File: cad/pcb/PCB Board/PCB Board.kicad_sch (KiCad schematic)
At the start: 14 parts, among them J1 Conn_01x02_Pin, J2 Conn_01x03_Pin, J3 Conn_01x04_Pin, J4 Conn_01x03_Pin, Q1 BC547, Q2 BC547, Q3 BC547, SW1 SW_Push, SW2 SW_Push, SW3 SW_Push, SW4 SW_Push

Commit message: started work on the pcb and cad data
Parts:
- removed J3: Conn_01x04_Pin, Connector_JST:JST_XH_B4B-XH-A_1x04_P2.50mm_Vertical, symbol Connector:Conn_01x04_Pin
- removed J4: Conn_01x03_Pin, Connector_JST:JST_XH_B3B-XH-A_1x03_P2.50mm_Vertical, symbol Connector:Conn_01x03_Pin
- removed Q1, Q2, Q3: BC547, Package_TO_SOT_THT:TO-92_Inline, symbol Transistor_BJT:BC547
- removed R1, R2, R3: R33K, Resistor_THT:R_Axial_DIN0204_L3.6mm_D1.6mm_P7.62mm_Horizontal, symbol Device:R
- added J3: Conn_01x02_Pin, Connector_Wire:SolderWire-0.1sqmm_1x02_P3.6mm_D0.4mm_OD1mm, symbol Connector:Conn_01x02_Pin
- added StepUp1: ~, Library:StepUp, symbol ReactPod:StepUp
- added U1: BOB-12009, BOB-12009:CONV_BOB-12009, symbol BOB-12009:BOB-12009
- added U2: ~, Library:Lolin32 Lite, symbol ReactPod:Lolin32
- J1: value Conn_01x02_Pin -> POWER
- J2: value Conn_01x03_Pin -> LED+
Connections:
- net at SW1.1, SW2.1, SW3.1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: now also J1.2 (Pin_2), J3.2 (Pin_2), StepUp1.1 (IN-), U1.GND_1 (GND), U1.GND_2 (GND), U2.GND
- net at SW1.2, SW2.2, SW3.2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: now also U2.18; no longer J1.2 (Pin_2)
- new net: J1.1 (Pin_1), J3.1 (Pin_1), StepUp1.2 (IN+)
- new net: J2.1 (Pin_1), U1.HV1
- new net: J2.2 (Pin_2), StepUp1.4 (OUT-)
- new net: J2.3 (Pin_3), StepUp1.3 (OUT+), U1.HV
- new net: U1.LV1, U2.19
- new net: U1.LV, U2.3V
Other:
- moved on the sheet: J2, SW1, SW2, SW3, SW4

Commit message: updated pcbs
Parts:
- added J4: ON_OFF_SWITCH, Connector_Wire:SolderWire-0.1sqmm_1x02_P3.6mm_D0.4mm_OD1mm_Relief, symbol Connector:Conn_01x02_Pin
- J3: value Conn_01x02_Pin -> BATTERY_CONNECTOR
- U1: value BOB-12009 -> Lvl-Shifter
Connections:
- net at J3.1 (Pin_1), StepUp1.2 (IN+): now also J4.1 (Pin_1); no longer J1.1 (Pin_1)
- new net: J1.1 (Pin_1), J4.2 (Pin_2)
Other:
- moved on the sheet: J1
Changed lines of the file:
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@@
 	(wire
 		(pts
-			(xy 12.7 33.02) (xy 12.7 157.48)
+			(xy 12.7 31.75) (xy 12.7 157.48)
 		)
 		(stroke
@@
 	(wire
 		(pts
-			(xy 46.99 30.48) (xy 48.26 30.48)
-		)
-		(stroke
-			(width 0)
-			(type default)
-		)
-	)
-	(wire
-		(pts
-			(xy 12.7 33.02) (xy 48.26 33.02)
+			(xy 19.05 24.13) (xy 48.26 24.13)
+		)
+		(stroke
+			(width 0)
+			(type default)
+		)
+	)
+	(wire
+		(pts
+			(xy 12.7 31.75) (xy 48.26 31.75)
 		)
 		(stroke
@@
 	(wire
 		(pts
-			(xy 48.26 26.67) (xy 57.15 26.67)
-		)
-		(stroke
-			(width 0)
-			(type default)
-		)
-	)
-	(wire
-		(pts
 			(xy 40.64 78.74) (xy 62.23 78.74)
 		)
@@
 	(wire
 		(pts
+			(xy 29.21 21.59) (xy 19.05 21.59)
+		)
+		(stroke
+			(width 0)
+			(type default)
+		)
+	)
+	(wire
+		(pts
 			(xy 69.85 173.99) (xy 62.23 173.99)
 		)
@@
 	(wire
 		(pts
-			(xy 48.26 27.94) (xy 48.26 26.67)
+			(xy 57.15 21.59) (xy 57.15 26.67)
 		)
 		(stroke
@@
 	(wire
 		(pts
-			(xy 46.99 27.94) (xy 48.26 27.94)
-		)
-		(stroke
-			(width 0)
-			(type default)
-		)
-	)
-	(wire
-		(pts
 			(xy 62.23 31.75) (xy 125.73 31.75)
 		)
@@
 	(wire
 		(pts
+			(xy 31.75 21.59) (xy 57.15 21.59)
+		)
+		(stroke
+			(width 0)
+			(type default)
+		)
+	)
+	(wire
+		(pts
 			(xy 157.48 26.67) (xy 189.23 26.67)
 		)
@@
 	(wire
 		(pts
-			(xy 48.26 33.02) (xy 48.26 31.75)
-		)
-		(stroke
-			(width 0)
-			(type default)
-		)
-	)
-	(wire
-		(pts
 			(xy 57.15 76.2) (xy 57.15 26.67)
 		)
@@
 	(wire
 		(pts
-			(xy 48.26 30.48) (xy 48.26 31.75)
+			(xy 48.26 24.13) (xy 48.26 31.75)
 		)
 		(stroke
@@
 		(length 2.54)
 		(shape round)
-		(at 29.21 33.02 0)
+		(at 29.21 31.75 0)
 		(fields_autoplaced yes)
 		(effects
@@
 		)
 		(property "Netclass" "GND"
-			(at 29.9085 30.48 0)
+			(at 29.9085 29.21 0)
 			(effects
 				(font
@@
 			)
 		)
-		(property "Value" "Conn_01x02_Pin"
+		(property "Value" "BATTERY_CONNECTOR"
 			(at 36.195 73.66 0)
 			(effects
@@
 	(symbol
 		(lib_id "Connector:Conn_01x02_Pin")
-		(at 41.91 27.94 0)
+		(at 31.75 16.51 270)
+		(unit 1)
+		(exclude_from_sim no)
+		(in_bom yes)
+		(on_board yes)
+		(dnp no)
+		(fields_autoplaced yes)
+		(property "Reference" "J4"
+			(at 33.02 15.8749 90)
+			(effects
+				(font
+					(size 1.27 1.27)
+				)
+				(justify left)
+			)
+		)
+		(property "Value" "ON_OFF_SWITCH"
+			(at 33.02 18.4149 90)
+			(effects
+				(font
+					(size 1.27 1.27)
+				)
+				(justify left)
+			)
+		)
+		(property "Footprint" "Connector_Wire:SolderWire-0.1sqmm_1x02_P3.6mm_D0.4mm_OD1mm_Relief"
+			(at 31.75 16.51 0)
+			(effects
+				(font
+					(size 1.27 1.27)
+				)
+				(hide yes)
+			)
+		)
+		(property "Datasheet" "~"
+			(at 31.75 16.51 0)
+			(effects
+				(font
+					(size 1.27 1.27)
+				)
+				(hide yes)
+			)
+		)
+		(property "Description" "Generic connector, single row, 01x02, script generated"
+			(at 31.75 16.51 0)
+			(effects
+				(font
+					(size 1.27 1.27)
+				)
+				(hide yes)
+			)
+		)
+		(pin "1"
+		)
+		(pin "2"
+		)
+		(instances
+			(project "PCB Board"
+				(path "/fdfca3f3-2f26-422d-bb5a-3dc9ec4c075c"
+					(reference "J4")
+					(unit 1)
+				)
+			)
+		)
+	)
+	(symbol
+		(lib_id "Connector:Conn_01x02_Pin")
+		(at 13.97 21.59 0)
 		(unit 1)
 		(exclude_from_sim no)
@@
 		(fields_autoplaced yes)
 		(property "Reference" "J1"
-			(at 42.545 22.86 0)
+			(at 14.605 16.51 0)
 			(effects
 				(font
@@
 		)
 		(property "Value" "POWER"
-			(at 42.545 25.4 0)
+			(at 14.605 19.05 0)
 			(effects
 				(font
@@
 		)
 		(property "Footprint" "Connector_JST:JST_XH_B2B-XH-A_1x02_P2.50mm_Vertical"
-			(at 41.91 27.94 0)
+			(at 13.97 21.59 0)
 			(effects
 				(font
@@
 		)
 		(property "Datasheet" "~"
-			(at 41.91 27.94 0)
+			(at 13.97 21.59 0)
 			(effects
 				(font
@@
 		)
 		(property "Description" "Generic connector, single row, 01x02, script generated"
-			(at 41.91 27.94 0)
+			(at 13.97 21.59 0)
 			(effects
 				(font
@@
 			)
 		)
-		(property "Value" "BOB-12009"
+		(property "Value" "Lvl-Shifter"
 			(at 166.37 76.2 0)
 			(effects

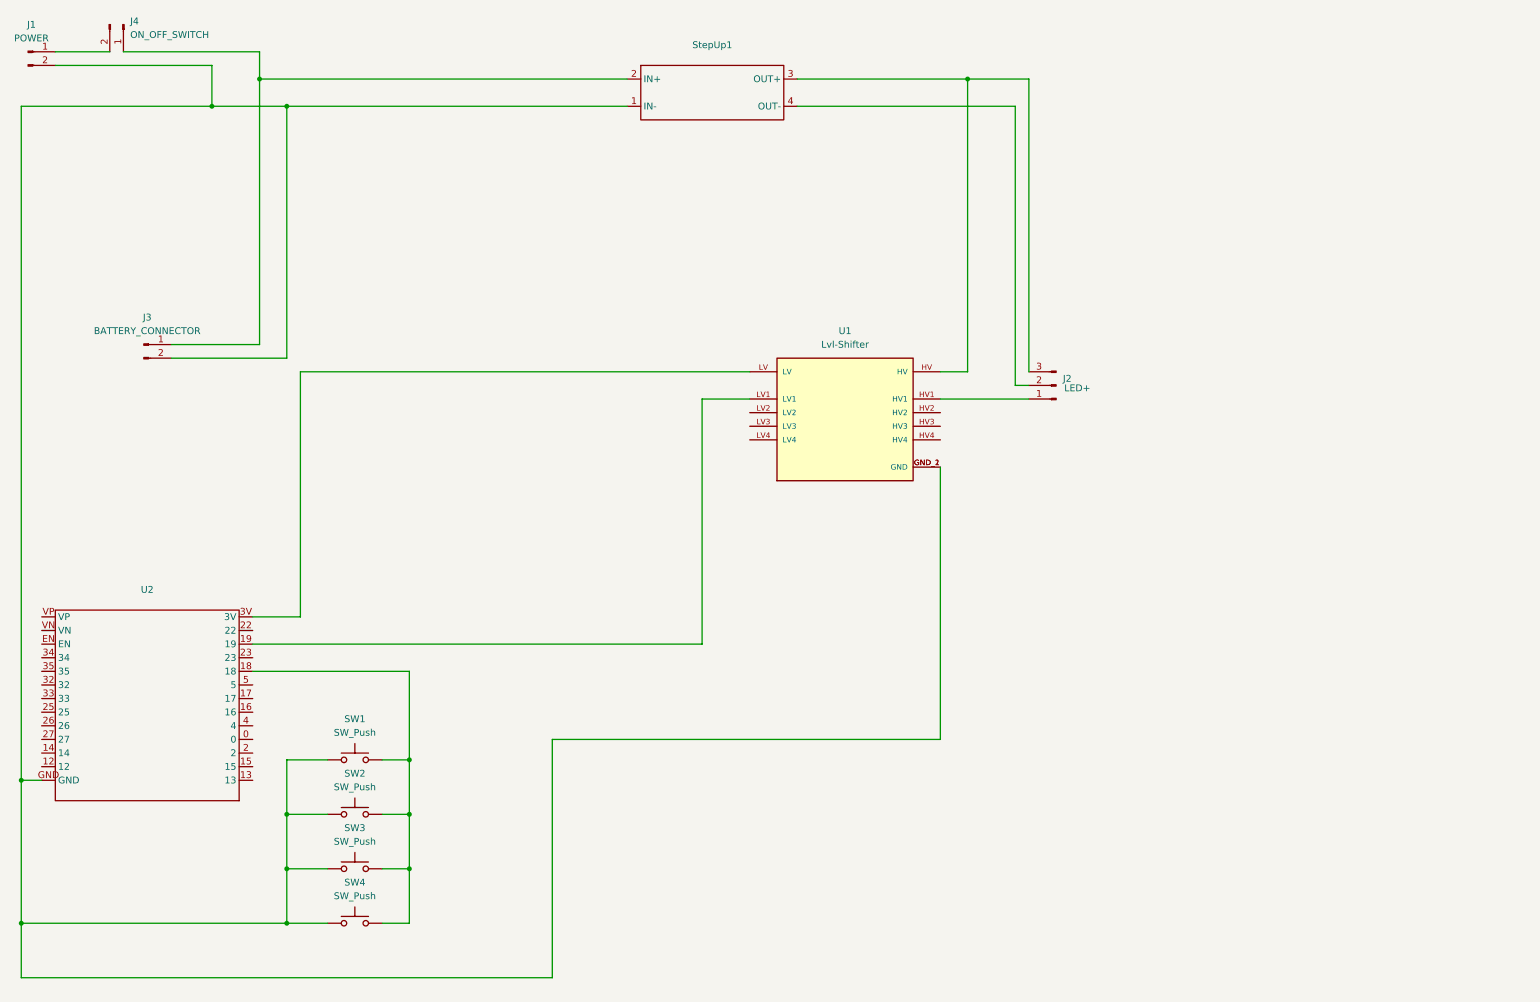
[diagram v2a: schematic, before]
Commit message: updated pcb design schematic
layouting missing. Also add on/off switch for battery (best solution with circumventing switch on charge
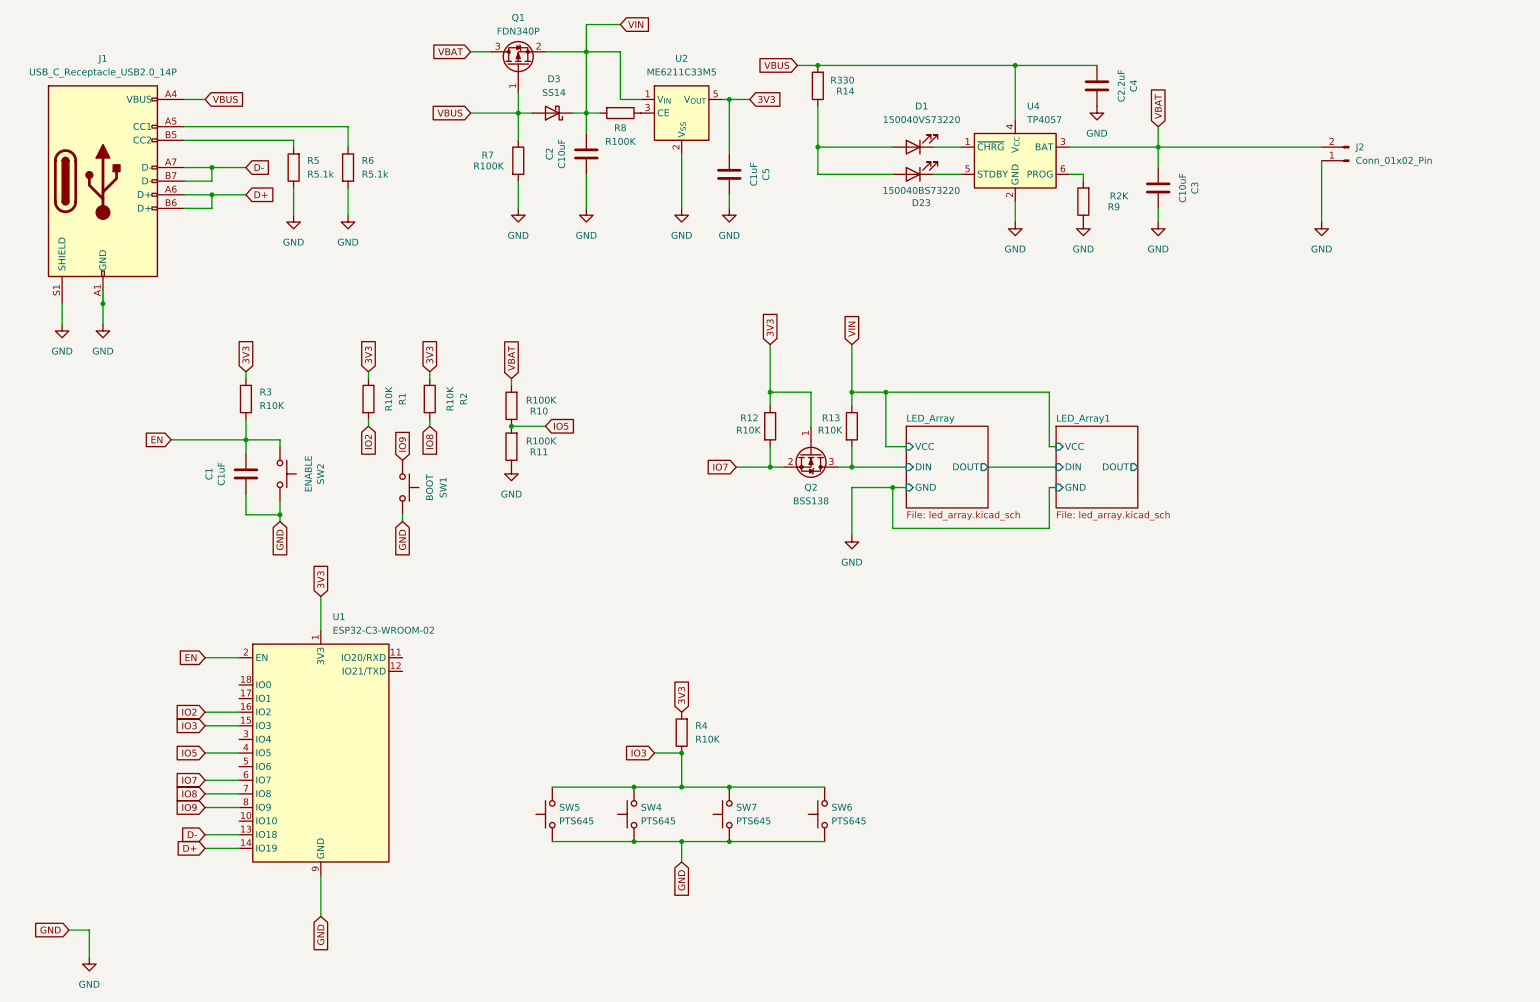
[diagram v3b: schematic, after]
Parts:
- removed J1: POWER, Connector_JST:JST_XH_B2B-XH-A_1x02_P2.50mm_Vertical, symbol Connector:Conn_01x02_Pin
- removed J2: LED+, Connector_JST:JST_XH_B3B-XH-A_1x03_P2.50mm_Vertical, symbol Connector:Conn_01x03_Pin
- removed J3: BATTERY_CONNECTOR, Connector_Wire:SolderWire-0.1sqmm_1x02_P3.6mm_D0.4mm_OD1mm, symbol Connector:Conn_01x02_Pin
- removed J4: ON_OFF_SWITCH, Connector_Wire:SolderWire-0.1sqmm_1x02_P3.6mm_D0.4mm_OD1mm_Relief, symbol Connector:Conn_01x02_Pin
- removed SW3: SW_Push, Button_Switch_THT:SW_PUSH_6mm_H5mm, symbol Switch:SW_Push
- removed StepUp1: ~, Library:StepUp, symbol ReactPod:StepUp
- removed U1: Lvl-Shifter, BOB-12009:CONV_BOB-12009, symbol BOB-12009:BOB-12009
- removed U2: ~, Library:Lolin32 Lite, symbol ReactPod:Lolin32
- added C1, C5: C1uF, Capacitor_SMD:C_0402_1005Metric, symbol Device:C
- added C2, C3: C10uF, Capacitor_SMD:C_0402_1005Metric, symbol Device:C
- added C4: C2.2uF, Capacitor_SMD:C_0402_1005Metric, symbol Device:C
- added D1: 150040VS73220, LED_SMD:LED_0402_1005Metric, symbol Device:LED
- added D23: 150040BS73220, LED_SMD:LED_0402_1005Metric, symbol Device:LED
- added D3: SS14, Diode_SMD:D_SMA, symbol Diode:SS14
- added J1: USB_C_Receptacle_USB2.0_14P, Connector_USB:USB_C_Receptacle_GCT_USB4105-xx-A_16P_TopMnt_Horizontal, symbol Connector:USB_C_Receptacle_USB2.0_14P
- added J2: Conn_01x02_Pin, Connector_JST:JST_PH_S2B-PH-K_1x02_P2.00mm_Horizontal, symbol Connector:Conn_01x02_Pin
- added Q1: FDN340P, Package_TO_SOT_SMD:SOT-23, symbol Transistor_FET:FDN340P
- added Q2: BSS138, Package_TO_SOT_SMD:SOT-23, symbol Transistor_FET:BSS138
- added R1, R12, R13, R2, R3, R4: R10K, Resistor_SMD:R_0402_1005Metric, symbol Device:R
- added R10, R11, R7, R8: R100K, Resistor_SMD:R_0402_1005Metric, symbol Device:R
- added R14: R330, Resistor_SMD:R_0402_1005Metric, symbol Device:R
- added R5, R6: R5.1k, Resistor_SMD:R_0402_1005Metric, symbol Device:R
- added R9: R2K, Resistor_SMD:R_0402_1005Metric, symbol Device:R
- added SW5, SW6, SW7: PTS645, Button_Switch_SMD:SW_SPST_PTS645, symbol Switch:SW_Push
- added U1: ESP32-C3-WROOM-02, RF_Module:ESP32-C3-WROOM-02, symbol RF_Module:ESP32-C3-WROOM-02
- added U2: ME6211C33M5, Package_TO_SOT_SMD:SOT-23-5, symbol Regulator_Linear:ME6211C33M5
- added U4: TP4057, Package_TO_SOT_SMD:TSOT-23-6, symbol Battery_Management:TP4057
- SW1: value SW_Push -> BOOT; footprint Button_Switch_THT:SW_PUSH_6mm_H5mm -> (none)
- SW2: value SW_Push -> ENABLE; footprint Button_Switch_THT:SW_PUSH_6mm_H5mm -> (none)
- SW4: value SW_Push -> PTS645; footprint Button_Switch_THT:SW_PUSH_6mm_H5mm -> Button_Switch_SMD:SW_SPST_PTS645
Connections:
- net GND: now reaches SW1.1, SW4.1
- net GND: now also SW2.2, C1.1, C2.1, C3.2, C4.2, C5.2, J1.A1 (GND), J1.A12 (GND), J1.B1 (GND), J1.B12 (GND), J1.S1 (SHIELD), J2.1 (Pin_1), R11.1, R5.1, R6.2, R7.2, R9.1, SW5.1, SW6.1, SW7.1, U1.19 (GND), U1.9 (GND), U2.2 (V_{SS}), U4.2 (GND); no longer SW2.1
- new net: J1.A5 (CC1), R6.1
- new net: J1.B5 (CC2), R5.2
- new net: R8.1, U2.3 (CE)
- new net: D1.1 (K), U4.1 (~{CHRG})
- new net: D23.1 (K), U4.5 (STDBY)
- new net: R9.2, U4.6 (PROG)
- new net: D1.2 (A), D23.2 (A), R14.1
- new net 3V3: C5.1, Q2.1 (G), R1.1, R12.1, R2.1, R3.2, R4.2, U1.1 (3V3), U2.5 (V_{OUT})
- new net D+: J1.A6 (D+), J1.B6 (D+), U1.14 (IO19)
- new net D-: J1.A7 (D-), J1.B7 (D-), U1.13 (IO18)
- new net EN: C1.2, R3.1, SW2.1, U1.2 (EN)
- new net IO2: R1.2, U1.16 (IO2)
- new net IO3: R4.1, SW4.2, SW5.2, SW6.2, SW7.2, U1.15 (IO3)
- new net IO5: R10.1, R11.2, U1.4 (IO5)
- new net IO7: Q2.2 (S), R12.2, U1.6 (IO7)
- new net IO8: R2.2, U1.7 (IO8)
- new net IO9: SW1.2, U1.8 (IO9)
- new net LED_Array/DIN: Q2.3 (D), R13.2
- new net VBAT: C3.1, J2.2 (Pin_2), Q1.3 (D), R10.2, U4.3 (BAT)
- new net VBUS: C4.1, D3.2 (A), J1.A4 (VBUS), J1.A9 (VBUS), J1.B4 (VBUS), J1.B9 (VBUS), Q1.1 (G), R14.2, R7.1, U4.4 (V_{CC})
- new net VIN: C2.2, D3.1 (K), Q1.2 (S), R13.1, R8.2, U2.1 (V_{IN})
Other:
- added sheet LED_Array (led_array.kicad_sch)
- added sheet LED_Array1 (led_array.kicad_sch)

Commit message: [WIP] save changes
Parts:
- added H2, H3, H4: MountingHole_Pad, MountingHole:MountingHole_3.2mm_M3_DIN965_Pad_TopBottom, symbol Mechanical:MountingHole_Pad
- added R14: R470, Resistor_SMD:R_0402_1005Metric, symbol Device:R
- added SW7: SLW-1277545-3A-RA-N-D, Button_Switch_THT:SW_Slide_SPDT_Angled_CK_OS102011MA1Q, symbol Switch:SW_Wuerth_450301014042
- C1: LCSC (none) -> C14445
- C2: LCSC (none) -> C77000
- C3: renamed from C5; LCSC (none) -> C14445
- C4: LCSC (none) -> C60078
- C5: renamed from C3; LCSC (none) -> C77000
- D1: renamed from D3; LCSC (none) -> C168859
- D2: renamed from D1; LCSC (none) -> C965793
- D3: renamed from D23; LCSC (none) -> C130724
- J1: value USB_C_Receptacle_USB2.0_14P -> USB4105
- J2: value Conn_01x02_Pin -> S2B-PH-K-S; LCSC (none) -> C173752
- SW1: renamed from SW2; value ENABLE -> PTS645; footprint (none) -> Button_Switch_SMD:SW_SPST_PTS645
- SW2: renamed from SW1; value BOOT -> PTS645; footprint (none) -> Button_Switch_SMD:SW_SPST_PTS645
- U2: value ME6211C33M5 -> TLV75533PDYDR; AltMPN (none) -> ME6211C33M5
- renumbered R3 to R1, R4 to R10, R14 to R11, R9 to R15, R5 to R2, R6 to R3, R1 to R4, R2 to R5, R10 to R6, R11 to R7, R7 to R8, R8 to R9, SW5 to SW3, SW7 to SW5, U4 to U3
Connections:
- net GND: now also H2.1, H3.1, H4.1, SW7.3 (A); no longer J2.1 (Pin_1)
- net LED_Array/DIN: now also R14.2; no longer Q2.3 (D), R13.2
- new net: Q2.3 (D), R13.2, R14.1
- new net: J2.1 (Pin_1), SW7.1 (B)
- no-connect marks 0 -> 9
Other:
- moved on the sheet: C5, J2, Q2, R12, R13

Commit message: updated schematic
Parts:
- Q1: LCSC (none) -> C75469
- Q2: LCSC (none) -> C52895
- R1, R10, R12, R13, R4, R5: LCSC (none) -> C25531
- R11: LCSC (none) -> C12246
- R14: LCSC (none) -> C25117
- R15: LCSC (none) -> C4109
- R2, R3: LCSC (none) -> C25905
- R6, R7, R8, R9: LCSC (none) -> C25530
- SW1, SW2, SW3, SW4, SW5, SW6: LCSC (none) -> C83206
- U1: LCSC (none) -> C2934560
- U2: LCSC (none) -> C28642215
- U3: LCSC (none) -> C440390
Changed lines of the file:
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@@
 			)
 		)
+		(property "LCSC" "C25905"
+			(at 73.66 43.18 0)
+			(effects
+				(font
+					(size 1.27 1.27)
+				)
+			)
+		)
 		(pin "1"
 		)
@@
 			)
 		)
+		(property "LCSC" "C25117"
+			(at 207.01 96.52 0)
+			(effects
+				(font
+					(size 1.27 1.27)
+				)
+			)
+		)
 		(pin "1"
 		)
@@
 			)
 		)
+		(property "LCSC" "C83206 "
+			(at 162.56 163.83 0)
+			(effects
+				(font
+					(size 1.27 1.27)
+				)
+			)
+		)
 		(pin "1"
 		)
@@
 			)
 		)
+		(property "LCSC" " C25531"
+			(at 135.89 148.59 0)
+			(effects
+				(font
+					(size 1.27 1.27)
+				)
+			)
+		)
 		(pin "1"
 		)
@@
 			)
 		)
+		(property "LCSC" "C83206 "
+			(at 60.96 100.33 0)
+			(effects
+				(font
+					(size 1.27 1.27)
+				)
+			)
+		)
 		(pin "1"
 		)
@@
 			)
 		)
+		(property "LCSC" " C25531"
+			(at 194.31 88.9 0)
+			(effects
+				(font
+					(size 1.27 1.27)
+				)
+			)
+		)
 		(pin "1"
 		)
@@
 			)
 		)
+		(property "LCSC" "C75469 "
+			(at 105.41 24.13 0)
+			(effects
+				(font
+					(size 1.27 1.27)
+				)
+			)
+		)
 		(pin "1"
 		)
@@
 			)
 		)
+		(property "LCSC" "C83206 "
+			(at 83.82 102.87 0)
+			(effects
+				(font
+					(size 1.27 1.27)
+				)
+			)
+		)
 		(pin "1"
 		)
@@
 			)
 		)
+		(property "LCSC" "C83206 "
+			(at 111.76 163.83 0)
+			(effects
+				(font
+					(size 1.27 1.27)
+				)
+			)
+		)
 		(pin "1"
 		)
@@
 			)
 		)
+		(property "LCSC" "C83206 "
+			(at 127 163.83 0)
+			(effects
+				(font
+					(size 1.27 1.27)
+				)
+			)
+		)
 		(pin "1"
 		)
@@
 			)
 		)
+		(property "LCSC" "C52895 "
+			(at 186.69 93.98 0)
+			(effects
+				(font
+					(size 1.27 1.27)
+				)
+			)
+		)
 		(pin "3"
 		)
@@
 			)
 		)
+		(property "LCSC" " C25531"
+			(at 179.07 88.9 0)
+			(effects
+				(font
+					(size 1.27 1.27)
+				)
+			)
+		)
 		(pin "1"
 		)
@@
 			)
 		)
+		(property "LCSC" " C25531"
+			(at 77.47 86.36 0)
+			(effects
+				(font
+					(size 1.27 1.27)
+				)
+			)
+		)
 		(pin "1"
 		)
@@
 			)
 		)
+		(property "LCSC" "C25530"
+			(at 124.46 33.02 0)
+			(effects
+				(font
+					(size 1.27 1.27)
+				)
+			)
+		)
 		(pin "1"
 		)
@@
 			)
 		)
+		(property "LCSC" " C440390"
+			(at 198.12 41.91 0)
+			(effects
+				(font
+					(size 1.27 1.27)
+				)
+			)
+		)
 		(pin "4"
 		)
@@
 			)
 		)
+		(property "LCSC" " C25531"
+			(at 54.61 86.36 0)
+			(effects
+				(font
+					(size 1.27 1.27)
+				)
+			)
+		)
 		(pin "1"
 		)
@@
 			)
 		)
+		(property "LCSC" "C25530"
+			(at 104.14 95.25 0)
+			(effects
+				(font
+					(size 1.27 1.27)
+				)
+			)
+		)
 		(pin "1"
 		)
@@
 			)
 		)
+		(property "LCSC" "C25530"
+			(at 105.41 41.91 0)
+			(effects
+				(font
+					(size 1.27 1.27)
+				)
+			)
+		)
 		(pin "1"
 		)
@@
 			)
 		)
+		(property "LCSC" " C28642215"
+			(at 135.89 33.02 0)
+			(effects
+				(font
+					(size 1.27 1.27)
+				)
+			)
+		)
 		(pin "3"
 		)
@@
 			)
 		)
+		(property "LCSC" "C12246"
+			(at 161.29 27.94 0)
+			(effects
+				(font
+					(size 1.27 1.27)
+				)
+			)
+		)
 		(pin "1"
 		)
@@
 			)
 		)
+		(property "LCSC" " C4109"
+			(at 210.82 49.53 0)
+			(effects
+				(font
+					(size 1.27 1.27)
+				)
+			)
+		)
 		(pin "1"
 		)
@@
 			)
 		)
+		(property "LCSC" "C2934560 "
+			(at 68.58 152.4 0)
+			(effects
+				(font
+					(size 1.27 1.27)
+				)
+			)
+		)
 		(pin "11"
 		)
@@
 			)
 		)
+		(property "LCSC" "C25905"
+			(at 63.5 43.18 0)
+			(effects
+				(font
+					(size 1.27 1.27)
+				)
+			)
+		)
 		(pin "1"
 		)
@@
 			)
 		)
+		(property "LCSC" " C25531"
+			(at 88.9 86.36 0)
+			(effects
+				(font
+					(size 1.27 1.27)
+				)
+			)
+		)
 		(pin "1"
 		)
@@
 			)
 		)
+		(property "LCSC" "C25530"
+			(at 104.14 87.63 0)
+			(effects
+				(font
+					(size 1.27 1.27)
+				)
+			)
+		)
 		(pin "1"
 		)
@@
 			)
 		)
+		(property "LCSC" "C83206 "
+			(at 144.78 163.83 0)
+			(effects
+				(font
+					(size 1.27 1.27)
+				)
+			)
+		)
